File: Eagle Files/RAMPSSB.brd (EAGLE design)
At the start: 94 x 80 mm, 30 parts, among them J10 1X2-3.5MM, J7 OSTTH020160, J9 1X2-3.5MM

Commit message: Update for publish
Final update before publish! Get ready!

Still needs some firmware work, but the hardware is there.
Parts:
- removed U$10: M05X2, RepRapjr:2X5
- added J17, J18, J19: (no value), SparkFun-Retired:1X02
- added LED1, LED2: (no value), adafruit:LED3MM
- added R1: (no value), adafruit:0207/7
- J9: value 1X2-3.5MM -> OSTTH020160; device adafruit:1X2-3.5MM -> con-ost:EDSTL130-02
- moved J10 9.06 mm to (89.8, 45.6)
- moved J9 9.02 mm to (88.9, 54.7)
- moved J4 2.54 mm to (67.3, 63.5)
- moved J1 2.54 mm to (67.3, 61.0)
- moved J5 2.54 mm to (67.3, 58.4)
- moved C1 1.27 mm to (88.9, 31.0)
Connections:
- new net LEDGND: LED1.K, LED2.K, R1.1
- new net RX: A-OUT.4, J19.2
- new net TX: A-OUT.3, J19.1
- net +5V: no longer U$10.1
- net GND: now also A-OUT.2, J17.2, J18.2, J9.2, R1.2, SERIAL.2; no longer J9.1
- net VCC: now also J9.1; no longer J9.2
- net VMOT: now also J17.1, J18.1
- net XPWM: now also LED1.A
- net YPWM: now also LED2.A
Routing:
- net +5V: track 76.8 -> 205.4 mm, vias 4 -> 6
- net GND: track 30.9 -> 63.6 mm
- net LEDGND: track 0.00 -> 27.1 mm
- net YPWM: track 28.4 -> 49.0 mm
- net VCC: track 41.4 -> 55.7 mm
- net XPWM: track 43.7 -> 55.6 mm
- net VMOT: track 0.00 -> 10.2 mm
- net XSTP: track 78.8 -> 86.7 mm
- net TX: track 0.00 -> 6.48 mm
- net RX: track 0.00 -> 6.48 mm
- net YEN: track 56.7 -> 61.7 mm
- net XDIR: track 72.4 -> 74.7 mm
- net XDIR2: track 45.2 -> 46.2 mm
- net XDIR1: track 44.8 -> 45.9 mm
- net YDIR: track 60.1 -> 61.1 mm
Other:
- outline, holes or cut-outs redrawn
- board text added: "200R"
- board text added: "CN1"
- board text added: "CN2"
- board text added: "Developed by S.Z."
- board text added: "R1"
- board text added: "RX"
- board text added: "TX"
- board text added: "X Y"
- board text removed: "(C) Scott Ziv"
- board text removed: "IN1"
- board text removed: "IN2"

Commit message: Updated firmware to run Arduino-GPIO to increase speed of digital writes
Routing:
- net GND: track 63.6 -> 50.6 mm, vias 2 -> 0
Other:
- board text added: "+ -"
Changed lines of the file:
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@@
 <layer number="17" name="Pads" color="2" fill="1" visible="yes" active="yes"/>
 <layer number="18" name="Vias" color="2" fill="1" visible="yes" active="yes"/>
-<layer number="19" name="Unrouted" color="13" fill="1" visible="yes" active="yes"/>
+<layer number="19" name="Unrouted" color="13" fill="1" visible="no" active="yes"/>
 <layer number="20" name="Dimension" color="15" fill="1" visible="yes" active="yes"/>
 <layer number="21" name="tPlace" color="7" fill="1" visible="yes" active="yes"/>
@@
 <text x="26.289" y="36.322" size="0.8128" layer="21" font="vector">TX</text>
 <text x="26.289" y="42.926" size="0.8128" layer="21" font="vector">RX</text>
+<text x="86.995" y="33.909" size="1.524" layer="21" font="vector">+ -</text>
 </plain>
 <attributes>
@@
 <signals>
 <signal name="GND">
-<contactref element="U$6" pad="GND@0"/>
 <contactref element="U$6" pad="GND"/>
-<contactref element="U$7" pad="GND@0"/>
 <contactref element="U$7" pad="GND"/>
 <contactref element="SER4" pad="1"/>
@@
 <vertex x="0" y="48.26"/>
 <vertex x="15.875" y="48.26"/>
-<vertex x="15.875" y="59.055"/>
-<vertex x="19.05" y="62.23"/>
-<vertex x="30.48" y="62.23"/>
+<vertex x="27.305" y="48.895"/>
+<vertex x="30.48" y="52.07"/>
 <vertex x="30.48" y="86.36"/>
 <vertex x="57.15" y="86.36"/>
@@
 <contactref element="MICRO1" pad="23"/>
 <contactref element="MICRO2" pad="23"/>
-<wire x1="1.27" y1="10.1601" x2="1.27" y2="11.09383125" width="0.4064" layer="16"/>
-<wire x1="2.4058" y1="13.8358" x2="5.08" y2="16.51" width="0.4064" layer="16"/>
-<wire x1="1.27" y1="11.09383125" x2="2.4058" y2="12.22963125" width="0.4064" layer="16"/>
-<wire x1="2.4058" y1="12.22963125" x2="2.4058" y2="13.8358" width="0.4064" layer="16"/>
-<via x="5.08" y="16.51" extent="1-16" drill="0.35"/>
-<wire x1="5.08" y1="16.51" x2="5.08" y2="21.59" width="0.4064" layer="1"/>
-<via x="5.08" y="21.59" extent="1-16" drill="0.35"/>
 <contactref element="J8" pad="2"/>
 <contactref element="J16" pad="2"/>
@@
 <contactref element="SERIAL" pad="2"/>
 <contactref element="A-OUT" pad="2"/>
+<contactref element="U$6" pad="GND@0"/>
+<contactref element="U$7" pad="GND@0"/>
+<wire x1="1.27" y1="10.1601" x2="1.27" y2="25.4001" width="0" layer="19" extent="1-1"/>
 </signal>
 <signal name="+5V">
@@
 <vertex x="0" y="48.26"/>
 <vertex x="15.5575" y="48.26"/>
-<vertex x="15.5575" y="58.7375"/>
-<vertex x="19.05" y="62.23"/>
-<vertex x="30.48" y="62.23"/>
+<vertex x="26.9875" y="48.5775"/>
+<vertex x="30.48" y="52.07"/>
 <vertex x="30.48" y="86.36"/>
 <vertex x="57.15" y="86.36"/>

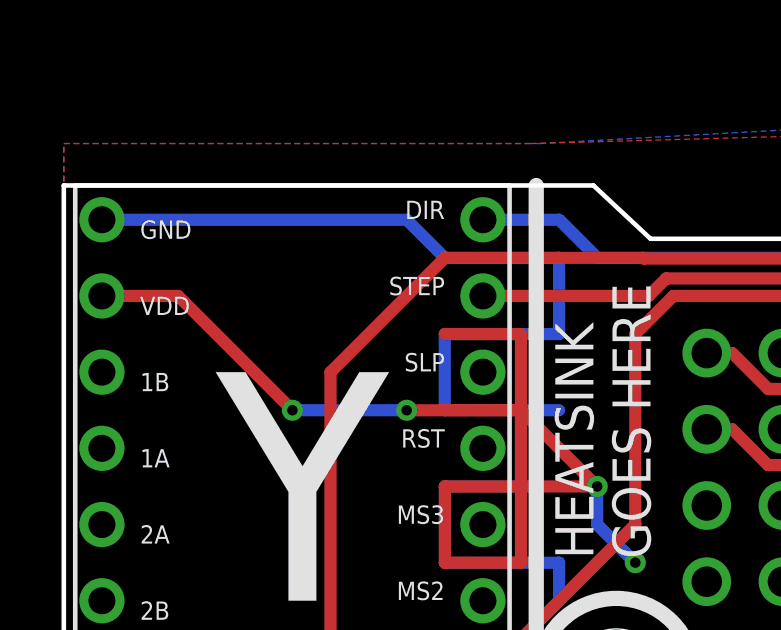
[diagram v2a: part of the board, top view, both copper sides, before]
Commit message: renamed PID_input to Error
Renamed "PID_Input" to "Error" which is more realistic
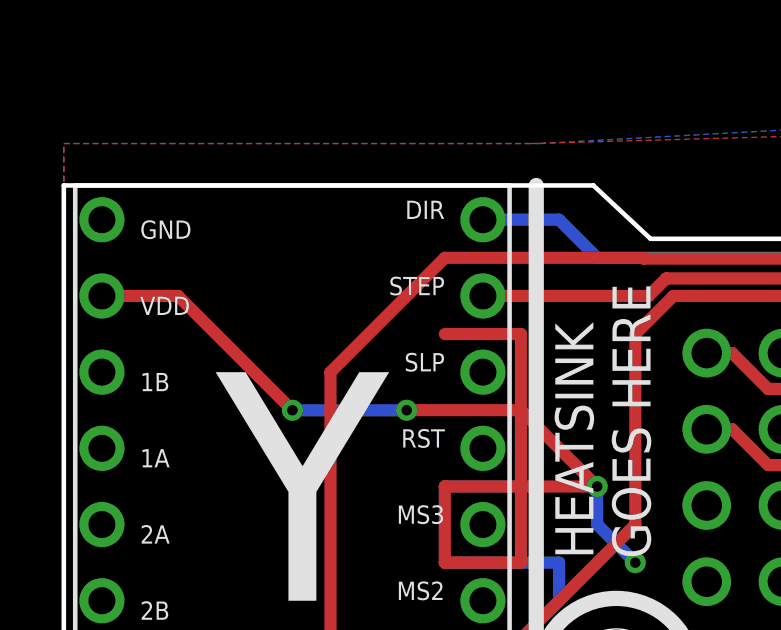
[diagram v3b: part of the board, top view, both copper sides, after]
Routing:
- net GND: track 50.6 -> 22.1 mm
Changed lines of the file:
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@@
 <signals>
 <signal name="GND">
-<contactref element="U$6" pad="GND"/>
-<contactref element="U$7" pad="GND"/>
 <contactref element="SER4" pad="1"/>
 <contactref element="J12" pad="3"/>
@@
 <contactref element="J16" pad="2"/>
 <contactref element="C1" pad="-"/>
-<wire x1="1.27" y1="45.72" x2="11.43" y2="45.72" width="0.4064" layer="16"/>
-<wire x1="11.43" y1="45.72" x2="12.7" y2="44.45" width="0.4064" layer="16"/>
-<wire x1="12.7" y1="44.45" x2="16.51" y2="44.45" width="0.4064" layer="16"/>
-<wire x1="16.51" y1="44.45" x2="16.51" y2="41.91" width="0.4064" layer="16"/>
-<wire x1="16.51" y1="41.91" x2="12.7" y2="41.91" width="0.4064" layer="16"/>
-<wire x1="12.7" y1="41.91" x2="12.7" y2="39.37" width="0.4064" layer="16"/>
-<wire x1="12.7" y1="39.37" x2="16.51" y2="39.37" width="0.4064" layer="16"/>
 <wire x1="15.24" y1="39.37" x2="15.24" y2="36.83" width="0.4064" layer="16"/>
 <wire x1="15.24" y1="36.83" x2="12.7" y2="36.83" width="0.4064" layer="16"/>
@@
 <contactref element="U$6" pad="GND@0"/>
 <contactref element="U$7" pad="GND@0"/>
+<contactref element="U$6" pad="GND"/>
+<contactref element="U$7" pad="GND"/>
 <wire x1="1.27" y1="10.1601" x2="1.27" y2="25.4001" width="0" layer="19" extent="1-1"/>
 </signal>
